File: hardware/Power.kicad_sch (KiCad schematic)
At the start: 14 parts, among them U2 TPS61023DRL

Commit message: more stuff
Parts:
- BT1: footprint Battery:BatteryHolder_Keystone_2466_1xAAA -> Connector_JST:JST_PH_S2B-PH-SM4-TB_1x02-1MP_P2.00mm_Horizontal; LCSC Part # (none) -> C47647
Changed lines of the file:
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@@
 			)
 		)
-		(property "Footprint" "Battery:BatteryHolder_Keystone_2466_1xAAA"
+		(property "Footprint" "Connector_JST:JST_PH_S2B-PH-SM4-TB_1x02-1MP_P2.00mm_Horizontal"
 			(at 38.1 58.166 90)
 			(effects
@@
 			(at 38.1 59.69 0)
 			(effects
+				(font
+					(size 1.27 1.27)
+				)
+				(hide yes)
+			)
+		)
+		(property "LCSC Part #" "C47647"
+			(at 38.1 59.69 0)
+			(effects

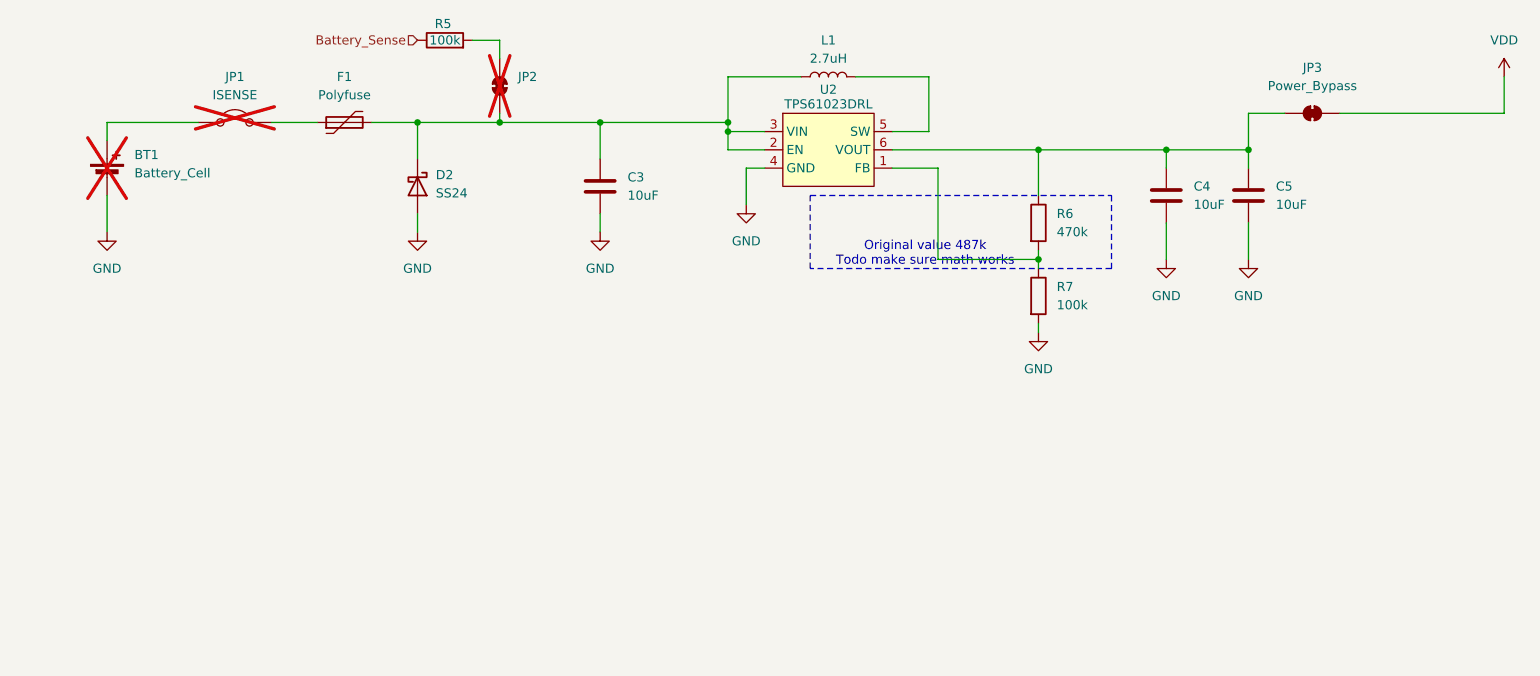
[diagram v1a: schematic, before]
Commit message: assigned part numbers and footprints
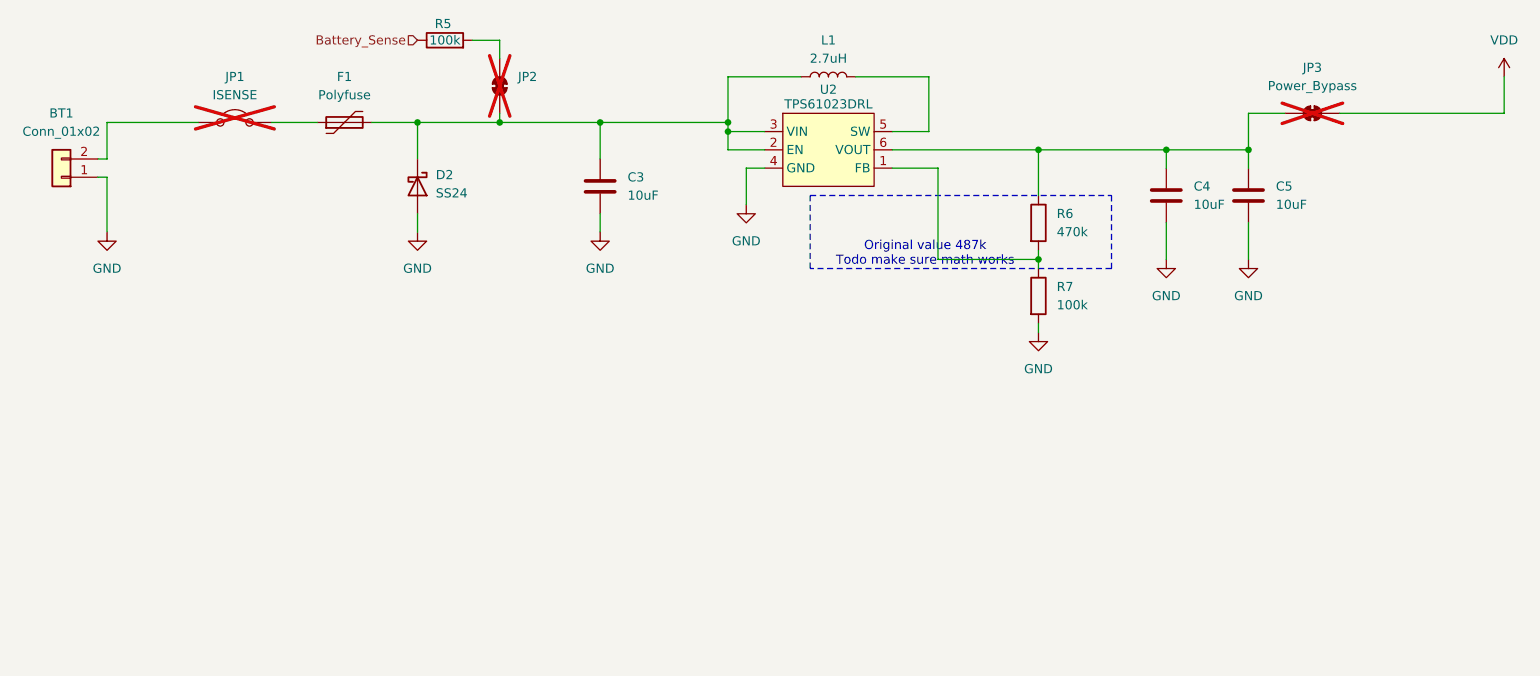
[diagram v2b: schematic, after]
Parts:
- BT1: value Battery_Cell -> Conn_01x02; symbol Device:Battery_Cell -> Connector_Generic:Conn_01x02; now fitted
- JP3: now not fitted
- R6: LCSC Part # (none) -> C23178
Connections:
- net GND: now also BT1.1 (Pin_1); no longer BT1.2 (-)
- net at JP1.1 (A): now also BT1.2 (Pin_2); no longer BT1.1 (+)
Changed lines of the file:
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@@
-	(wire
-		(pts
-			(xy 38.1 62.23) (xy 38.1 67.31)
-		)
-		(stroke
-			(width 0)
-			(type default)
-		)
-	)
 	(wire
 		(pts
@@
 	(wire
 		(pts
+			(xy 38.1 52.07) (xy 38.1 57.15)
+		)
+		(stroke
+			(width 0)
+			(type default)
+		)
+	)
+	(wire
+		(pts
+			(xy 38.1 59.69) (xy 38.1 67.31)
+		)
+		(stroke
+			(width 0)
+			(type default)
+		)
+	)
+	(wire
+		(pts
 			(xy 201.93 50.8) (xy 196.85 50.8)
 		)
@@
 	(wire
 		(pts
-			(xy 38.1 52.07) (xy 38.1 54.61)
-		)
-		(stroke
-			(width 0)
-			(type default)
-		)
-	)
-	(wire
-		(pts
 			(xy 38.1 52.07) (xy 50.8 52.07)
 		)
@@
 	(wire
 		(pts
+			(xy 38.1 57.15) (xy 36.83 57.15)
+		)
+		(stroke
+			(width 0)
+			(type default)
+		)
+	)
+	(wire
+		(pts
 			(xy 74.93 52.07) (xy 81.28 52.07)
 		)
@@
 		(pts
 			(xy 81.28 64.77) (xy 81.28 67.31)
+		)
+		(stroke
+			(width 0)
+			(type default)
+		)
+	)
+	(wire
+		(pts
+			(xy 36.83 59.69) (xy 38.1 59.69)
 		)
 		(stroke
@@
 		(in_bom no)
 		(on_board yes)
-		(dnp no)
+		(dnp yes)
 		(fields_autoplaced yes)
 		(property "Reference" "JP3"
@@
 	)
 	(symbol
-		(lib_id "Device:Battery_Cell")
-		(at 38.1 59.69 0)
+		(lib_id "Connector_Generic:Conn_01x02")
+		(at 31.75 59.69 180)
 		(unit 1)
 		(exclude_from_sim no)
 		(in_bom yes)
 		(on_board yes)
-		(dnp yes)
+		(dnp no)
 		(fields_autoplaced yes)
 		(property "Reference" "BT1"
-			(at 41.91 56.5784 0)
-			(effects
-				(font
-					(size 1.27 1.27)
-				)
-				(justify left)
-			)
-		)
-		(property "Value" "Battery_Cell"
-			(at 41.91 59.1184 0)
-			(effects
-				(font
-					(size 1.27 1.27)
-				)
-				(justify left)
+			(at 31.75 50.8 0)
+			(effects
+				(font
+					(size 1.27 1.27)
+				)
+			)
+		)
+		(property "Value" "Conn_01x02"
+			(at 31.75 53.34 0)
+			(effects
+				(font
+					(size 1.27 1.27)
+				)
 			)
 		)
 		(property "Footprint" "Connector_JST:JST_PH_S2B-PH-SM4-TB_1x02-1MP_P2.00mm_Horizontal"
-			(at 38.1 58.166 90)
+			(at 31.75 59.69 0)
 			(effects
 				(font
@@
 		)
 		(property "Datasheet" "~"
-			(at 38.1 58.166 90)
-			(effects
-				(font
-					(size 1.27 1.27)
-				)
-				(hide yes)
-			)
-		)
-		(property "Description" "Single-cell battery"
-			(at 38.1 59.69 0)
+			(at 31.75 59.69 0)
+			(effects
+				(font
+					(size 1.27 1.27)
+				)
+				(hide yes)
+			)
+		)
+		(property "Description" "Generic connector, single row, 01x02, script generated (kicad-library-utils/schlib/autogen/connector/)"
+			(at 31.75 59.69 0)
 			(effects
 				(font
@@
 		)
 		(property "DK #" "36-2466-ND"
-			(at 38.1 59.69 0)
+			(at 31.75 59.69 0)
 			(effects
 				(font
@@
 		)
 		(property "JLCPCB Rotation Offset" ""
-			(at 38.1 59.69 0)
+			(at 31.75 59.69 0)
 			(effects
 				(font
@@
 		)
 		(property "Cost" ""
-			(at 38.1 59.69 0)
+			(at 31.75 59.69 0)
 			(effects
 				(font
@@
 		)
 		(property "LCSC Part #" "C47647"
-			(at 38.1 59.69 0)
+			(at 31.75 59.69 0)
 			(effects
 				(font
@@
 			(at 167.64 66.04 0)
 			(effects
+				(font
+					(size 1.27 1.27)
+				)
+				(hide yes)
+			)
+		)
+		(property "LCSC Part #" "C23178 "
+			(at 167.64 66.04 0)
+			(effects

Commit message: stuff
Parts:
- added C20, C21: 1uF, Capacitor_SMD:C_0805_2012Metric, symbol Device:C
- added U5: XC6206PxxxMR, Package_TO_SOT_SMD:SOT-23-3, symbol Regulator_Linear:XC6206PxxxMR
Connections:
- net GND: now also C20.1, C21.1, U5.1 (GND)
- net VDD renamed +4V
- net +4V: now also C20.2, U5.3 (VI)
- new net +3V3: C21.2, U5.2 (VO)

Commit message: layout
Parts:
- R5, R7: footprint Resistor_SMD:R_0603_1608Metric -> Resistor_SMD:R_0402_1005Metric; LCSC Part # C25803 -> C25741
- R6: footprint Resistor_SMD:R_0603_1608Metric -> Resistor_SMD:R_0402_1005Metric; LCSC Part # C23178 -> C25790
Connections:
- net 4V_REG: now reaches C4.1, C5.1, JP3.1 (A), R6.1, U2.6 (VOUT)
- net +BATT: now reaches C3.1, D2.1 (K), F1.2, JP2.1 (A), L1.1, U2.2 (EN), U2.3 (VIN)
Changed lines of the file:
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@@
+	)
+	(junction
+		(at 102.87 52.07)
+		(diameter 0)
+		(color 0 0 0 0)
 	)
 	(junction
@@
 	(wire
 		(pts
-			(xy 92.71 52.07) (xy 106.68 52.07)
+			(xy 92.71 52.07) (xy 102.87 52.07)
 		)
 		(stroke
@@
 	(wire
 		(pts
+			(xy 102.87 52.07) (xy 106.68 52.07)
+		)
+		(stroke
+			(width 0)
+			(type default)
+		)
+	)
+	(wire
+		(pts
 			(xy 196.85 66.04) (xy 196.85 71.12)
 		)
@@
 		(pts
 			(xy 153.67 58.42) (xy 153.67 71.12)
+		)
+		(stroke
+			(width 0)
+			(type default)
+		)
+	)
+	(wire
+		(pts
+			(xy 102.87 48.26) (xy 102.87 52.07)
 		)
 		(stroke
@@
 				(size 1.27 1.27)
 			)
+		)
+	)
+	(label "4V_REG"
+		(at 173.99 55.88 0)
+		(effects
+			(font
+				(size 1.27 1.27)
+			)
+			(justify left bottom)
 		)
 	)
@@
 			)
 		)
-		(property "Footprint" "Resistor_SMD:R_0603_1608Metric"
+		(property "Footprint" "Resistor_SMD:R_0402_1005Metric"
 			(at 165.862 76.2 90)
 			(effects
@@
 			)
 		)
-		(property "LCSC Part #" "C25803"
+		(property "LCSC Part #" "C25741"
 			(at 167.64 76.2 0)
 			(effects
@@
 	)
 	(symbol
+		(lib_id "power:+BATT")
+		(at 102.87 48.26 0)
+		(unit 1)
+		(exclude_from_sim no)
+		(in_bom yes)
+		(on_board yes)
+		(dnp no)
+		(fields_autoplaced yes)
+		(property "Reference" "#PWR46"
+			(at 102.87 52.07 0)
+			(effects
+				(font
+					(size 1.27 1.27)
+				)
+				(hide yes)
+			)
+		)
+		(property "Value" "+BATT"
+			(at 102.87 43.18 0)
+			(effects
+				(font
+					(size 1.27 1.27)
+				)
+			)
+		)
+		(property "Footprint" ""
+			(at 102.87 48.26 0)
+			(effects
+				(font
+					(size 1.27 1.27)
+				)
+				(hide yes)
+			)
+		)
+		(property "Datasheet" ""
+			(at 102.87 48.26 0)
+			(effects
+				(font
+					(size 1.27 1.27)
+				)
+				(hide yes)
+			)
+		)
+		(property "Description" "Power symbol creates a global label with name \"+BATT\""
+			(at 102.87 48.26 0)
+			(effects
+				(font
+					(size 1.27 1.27)
+				)
+				(hide yes)
+			)
+		)
+		(pin "1"
+		)
+		(instances
+			(project ""
+				(path "/3313c311-f70a-45a8-bbf4-c9e4cbd18d5c/d0acc147-0fef-4ef7-a17f-f3392f92d847"
+					(reference "#PWR46")
+					(unit 1)
+				)
+			)
+		)
+	)
+	(symbol
 		(lib_id "power:GND")
 		(at 127 63.5 0)
@@
 			)
 		)
-		(property "Footprint" "Resistor_SMD:R_0603_1608Metric"
+		(property "Footprint" "Resistor_SMD:R_0402_1005Metric"
 			(at 165.862 66.04 90)
 			(effects
@@
 			)
 		)
-		(property "LCSC Part #" "C23178 "
+		(property "LCSC Part #" "C25790"
 			(at 167.64 66.04 0)
 			(effects
@@
 			)
 		)
-		(property "Footprint" "Resistor_SMD:R_0603_1608Metric"
+		(property "Footprint" "Resistor_SMD:R_0402_1005Metric"
 			(at 85.09 42.418 90)
 			(effects
@@
 			)
 		)
-		(property "LCSC Part #" "C25803"
+		(property "LCSC Part #" "C25741"
 			(at 85.09 40.64 0)
 			(effects

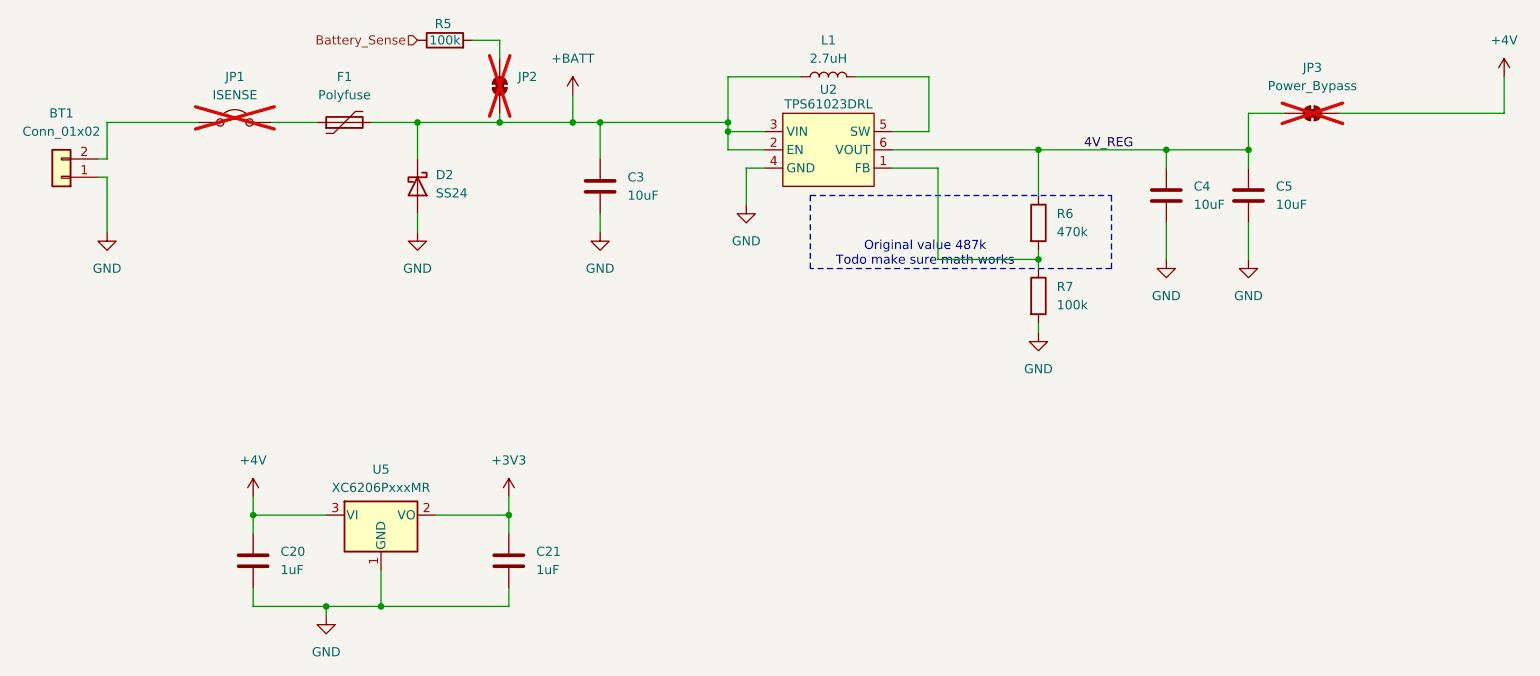
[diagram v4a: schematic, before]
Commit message: redid design based on STM3201
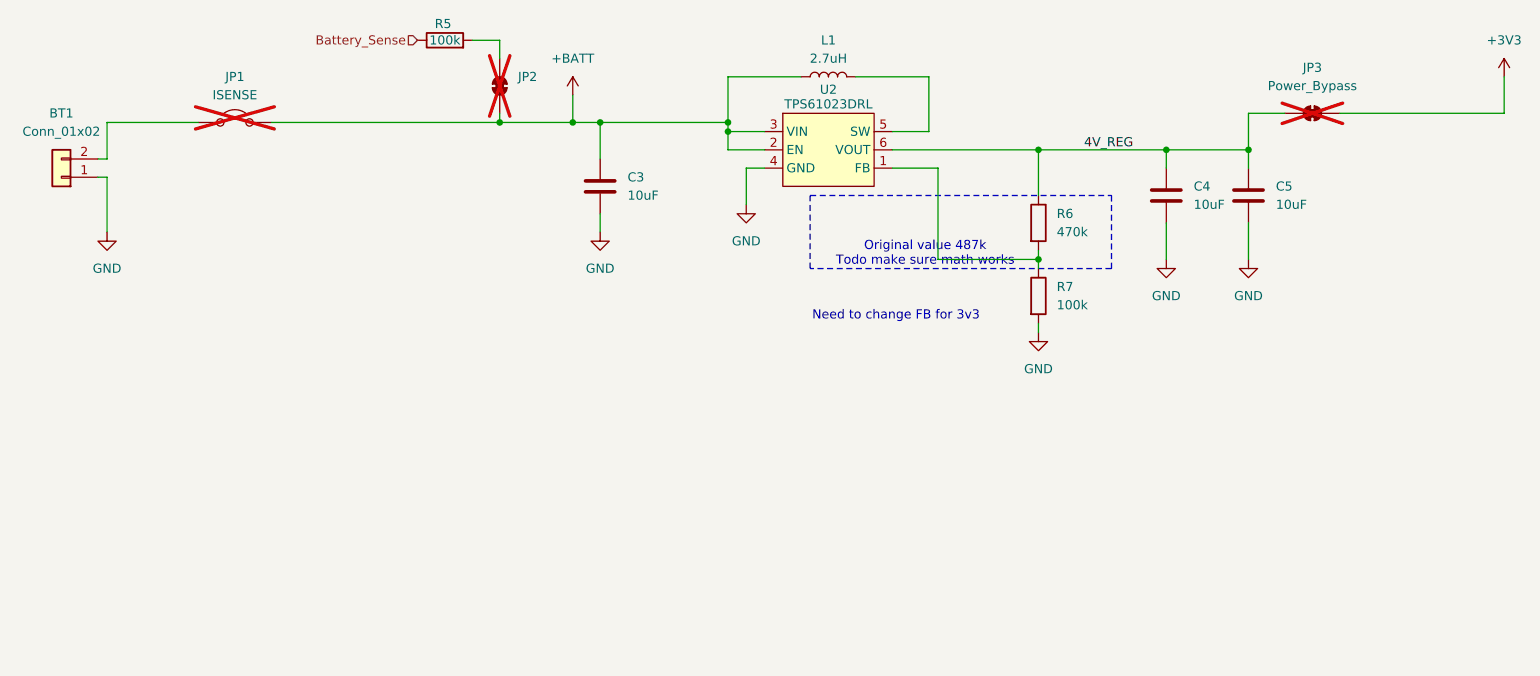
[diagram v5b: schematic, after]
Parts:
- removed C20, C21: 1uF, Capacitor_SMD:C_0805_2012Metric, symbol Device:C
- removed D2: SS24, Diode_SMD:D_SMA, symbol Device:D_Schottky
- removed F1: Polyfuse, Fuse:Fuse_1206_3216Metric, symbol Device:Polyfuse
- removed U5: XC6206PxxxMR, Package_TO_SOT_SMD:SOT-23-3, symbol Regulator_Linear:XC6206PxxxMR
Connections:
- net +4V is gone; now on net +3V3: JP3.2 (B)
- net +BATT: now also JP1.2 (B)
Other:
- note added: "Need to change FB for 3v3"

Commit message: design polishing
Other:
- note added: "Need to change FB for 3v3 (should be 453k)"
- note removed: "Need to change FB for 3v3"
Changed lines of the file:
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@@
 		)
 	)
-	(text "Need to change FB for 3v3"
+	(text "Need to change FB for 3v3\n(should be 453k)"
 		(exclude_from_sim no)
 		(at 147.828 78.994 0)
@@
 			)
 		)
-		(property "Datasheet" ""
+		(property "Datasheet" "https://www.ti.com/lit/ds/symlink/tps61023.pdf"
 			(at 138.43 50.8 0)
 			(effects

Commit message: stuff
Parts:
- added C11, C12: 1uF, Capacitor_SMD:C_0805_2012Metric, symbol Device:C
- added U4: XC6206PxxxMR, Package_TO_SOT_SMD:SOT-23-3, symbol Regulator_Linear:XC6206PxxxMR
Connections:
- net +3V3: now also C12.2, U4.2 (VO)
- net GND: now also C11.1, C12.1, U4.1 (GND)
- new net VBUS: C11.2, U4.3 (VI)

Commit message: schematic is kinda finished now
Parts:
- removed BT1: Conn_01x02, Connector_JST:JST_PH_S2B-PH-SM4-TB_1x02-1MP_P2.00mm_Horizontal, symbol Connector_Generic:Conn_01x02
- added BT1: Battery_Cell, Battery:BatteryHolder_Keystone_3002_1x2032, symbol Device:Battery_Cell
- added C13, C14: 0.1uF, Capacitor_SMD:C_0402_1005Metric, symbol Device:C
- added R10: 470, Resistor_SMD:R_0402_1005Metric, symbol Device:R
- added U5: TOS2115ADRBT, Package_SON:VSON-8-1EP_3x3mm_P0.65mm_EP1.65x2.4mm, symbol cat:TPS2115ADRBT
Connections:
- net +3V3: now also U5.7 (OUT); no longer C12.2, JP3.2 (B), U4.2 (VO)
- net GND: now also BT1.2 (-), C13.1, C14.1, R10.2, U5.3 (D1), U5.5 (GND), U5.9 (GND)
- net at JP1.1 (A): now also BT1.1 (+)
- net 4V_REG renamed 3V3_REG
- new net: R10.1, U5.4 (ILIM)
- new net 3V3_BATT: C14.2, JP3.2 (B), U5.6 (IN2)
- new net 3V3_USB: C12.2, C13.2, U4.2 (VO), U5.8 (IN1)
- no-connect marks 0 -> 2
